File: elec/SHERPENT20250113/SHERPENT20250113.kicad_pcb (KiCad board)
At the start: 4 copper layers, 99 parts, among them J1 2137160001, J2 Conn_01x02_Socket, J3 Conn_01x03_Socket, J4 Conn_01x03_Socket, Q1 NMOS, Q2 PMOS, SW1 SW_Push, U1 AN034_ANTENNA, U2 MCP73831T-2ACI_OT, U3 TPS61288LRQQR, U4 TPS7A2633DRVR, U5 LM66200DRLR, U6 ESP32-C3, U7 W25Q128JVS, Y1 40MHz

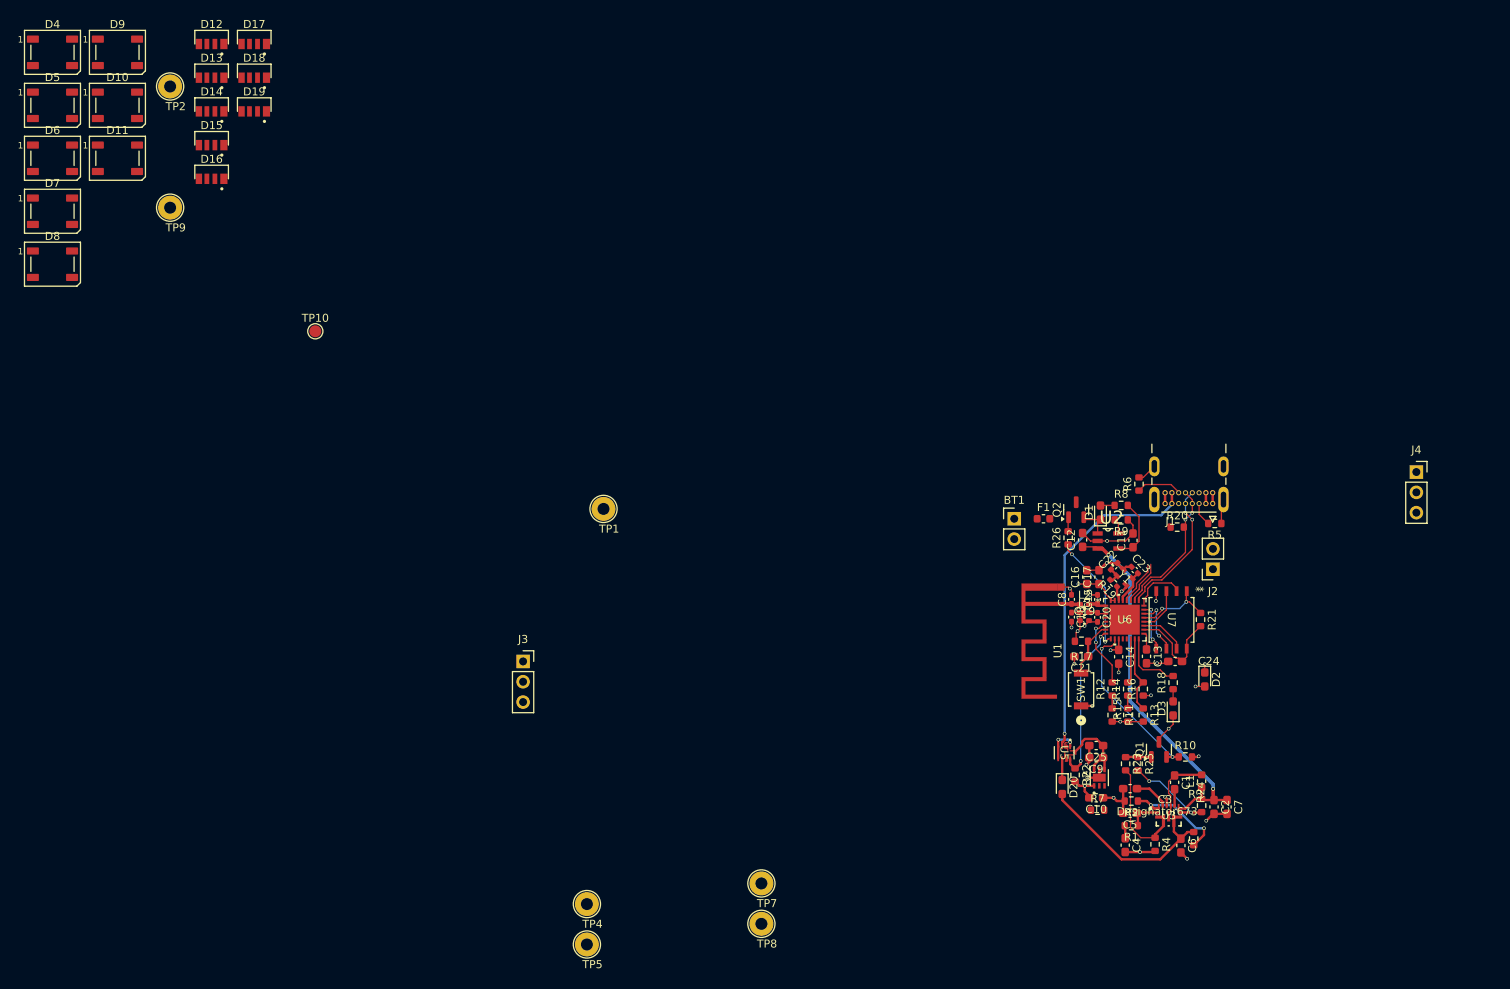
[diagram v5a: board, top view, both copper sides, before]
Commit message: Ajout des LED sur le pcb
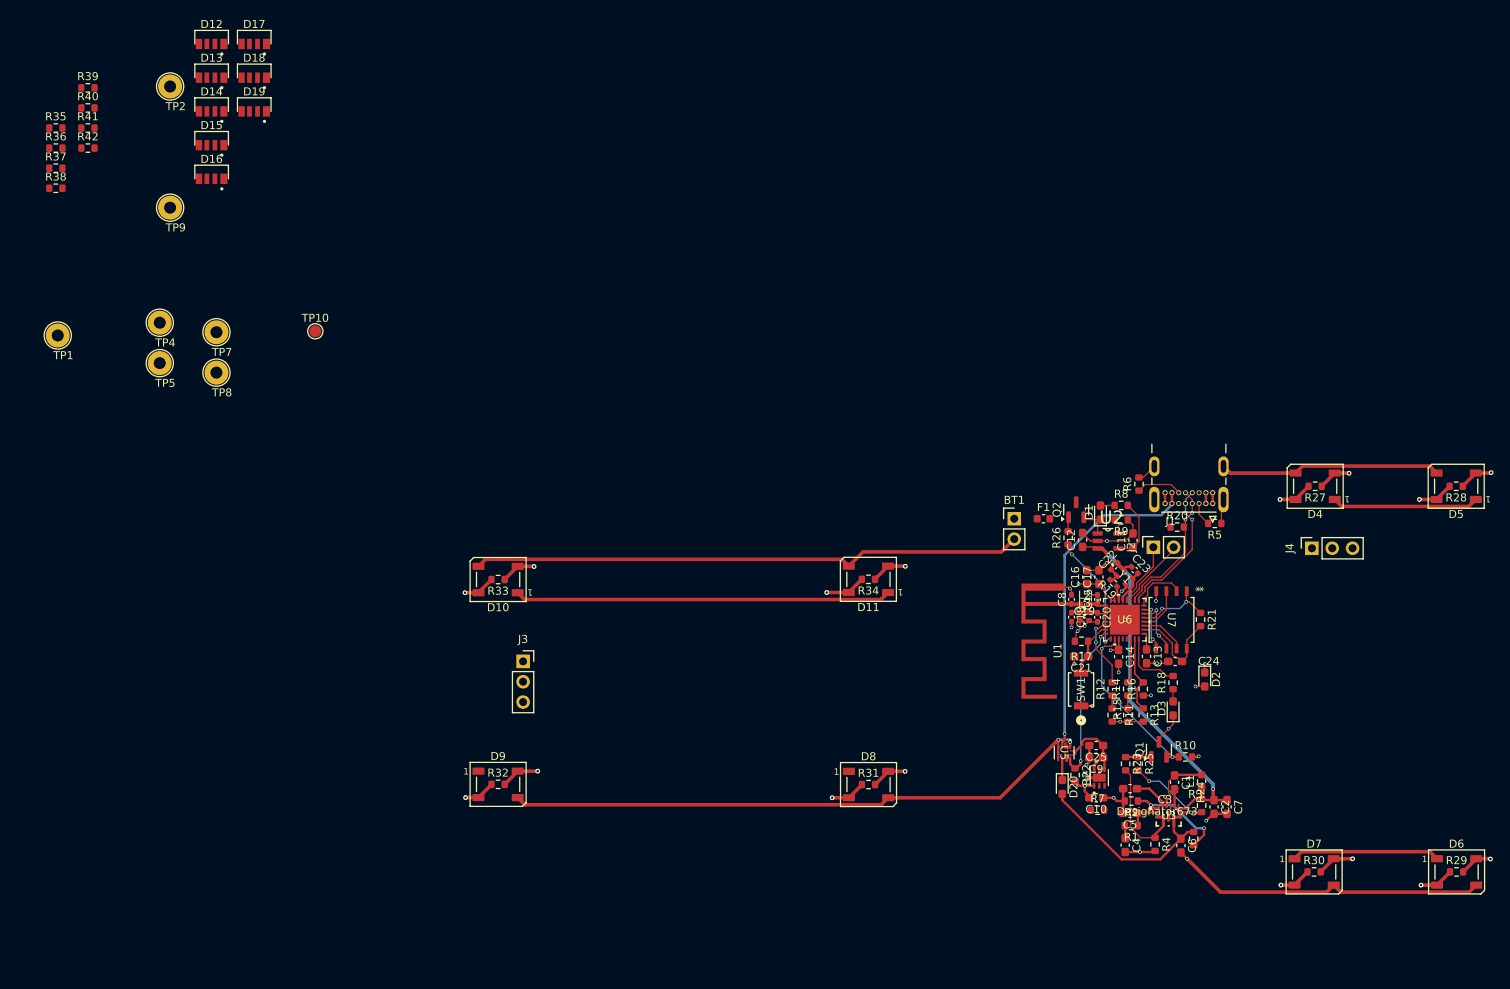
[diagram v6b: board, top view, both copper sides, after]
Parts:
- added R27: 0, Resistor_SMD:R_0603_1608Metric, F.Cu at (184.1, 78.5)
- added R28: 0, Resistor_SMD:R_0603_1608Metric, F.Cu at (201.7, 78.5)
- added R29: 0, Resistor_SMD:R_0603_1608Metric, F.Cu at (201.8, 126.7)
- added R30: 0, Resistor_SMD:R_0603_1608Metric, F.Cu at (184.0, 126.7)
- added R31: 0, Resistor_SMD:R_0603_1608Metric, F.Cu at (128.3, 115.8)
- added R32: 0, Resistor_SMD:R_0603_1608Metric, F.Cu at (82.0, 115.7)
- added R33: 0, Resistor_SMD:R_0603_1608Metric, F.Cu at (82.0, 90.1)
- added R34: 0, Resistor_SMD:R_0603_1608Metric, F.Cu at (128.3, 90.1)
- added R35: 0, Resistor_SMD:R_0603_1608Metric, F.Cu at (26.7, 33.7)
- added R36: 0, Resistor_SMD:R_0603_1608Metric, F.Cu at (26.7, 36.2)
- added R37: 0, Resistor_SMD:R_0603_1608Metric, F.Cu at (26.7, 38.7)
- added R38: 0, Resistor_SMD:R_0603_1608Metric, F.Cu at (26.7, 41.2)
- added R39: 0, Resistor_SMD:R_0603_1608Metric, F.Cu at (30.7, 28.7)
- added R40: 0, Resistor_SMD:R_0603_1608Metric, F.Cu at (30.7, 31.2)
- added R41: 0, Resistor_SMD:R_0603_1608Metric, F.Cu at (30.7, 33.7)
- added R42: 0, Resistor_SMD:R_0603_1608Metric, F.Cu at (30.7, 36.2)
- moved D6 196.9 mm to (201.8, 126.7)
- moved D5 181.8 mm to (201.7, 78.5), turned to 180 degrees
- moved D7 178.0 mm to (184.0, 126.7)
- moved D4 166.9 mm to (184.1, 78.5), turned to 180 degrees
- moved D8 121.0 mm to (128.3, 115.8)
- moved D11 107.6 mm to (128.3, 90.1), turned to 180 degrees
- moved D9 103.1 mm to (82.0, 115.7)
- moved TP7 96.9 mm to (46.8, 59.2)
- moved TP8 96.9 mm to (46.8, 64.3)
- moved TP4 90.2 mm to (39.7, 58.0)
- moved TP5 90.2 mm to (39.7, 63.1)
- moved D10 76.0 mm to (82.0, 90.1), turned to 180 degrees
- moved TP1 71.6 mm to (26.9, 59.6)
- moved J4 16.2 mm to (183.7, 86.2), turned to 90 degrees
- moved J2 7.94 mm to (163.9, 86.1), turned to 90 degrees
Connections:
- D19 pad 3: Net-(D19-DOUT) -> /I2C_DI
- D4 pad 4: /NEO -> /I2C_DO
- TP10 pad 1: Net-(D19-DOUT) -> /I2C_DI
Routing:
- net GND: track 76.5 -> 283.5 mm
- net Net-(D5-DOUT): track 0.00 -> 111.5 mm, vias 0 -> 2
- net +5V: track 0.00 -> 83.9 mm
- net Net-(D7-DOUT): track 0.00 -> 61.4 mm, vias 0 -> 2
- net Net-(D8-DOUT): track 0.00 -> 47.4 mm, vias 0 -> 2
- net Net-(D10-DOUT): track 0.00 -> 47.4 mm, vias 0 -> 2
- net Net-(D10-DIN): track 0.00 -> 33.6 mm, vias 0 -> 2
- net /I2C_DO: track 5.56 -> 28.9 mm, vias 0 -> 1
- net Net-(D6-DOUT): track 0.00 -> 18.9 mm, vias 0 -> 2
- net Net-(D4-DOUT): track 0.00 -> 18.7 mm, vias 0 -> 2
- net Net-(D11-DOUT): track 0.00 -> 4.50 mm, vias 0 -> 1
- net /I2C_DI: track 5.52 -> 8.35 mm

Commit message: Ajout de step
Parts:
- removed D12, D13, D14, D15, D16, D17, D18, D19: WS2812B4020, Library:WS2812B4020
- removed R35, R36, R37, R38, R39, R40, R41, R42: 0, Resistor_SMD:R_0603_1608Metric
- removed TP1, TP2, TP4, TP5, TP7, TP8, TP9: TestPoint, TestPoint:TestPoint_Loop_D2.54mm_Drill1.5mm_Beaded
- removed TP10: TestPoint, TestPoint:TestPoint_Pad_D1.5mm
- added REF**: MountingHole_3.5mm, MountingHole:MountingHole_3.5mm, F.Cu at (139.0, 129.0)
- added REF**: MountingHole_3.5mm, MountingHole:MountingHole_3.5mm, F.Cu at (157.0, 129.0)
- added REF**: MountingHole_3.5mm, MountingHole:MountingHole_3.5mm, F.Cu at (139.0, 77.0)
- added REF**: MountingHole_3.5mm, MountingHole:MountingHole_3.5mm, F.Cu at (157.0, 77.0)
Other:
- board outline added: 130.2 x 60.2 mm

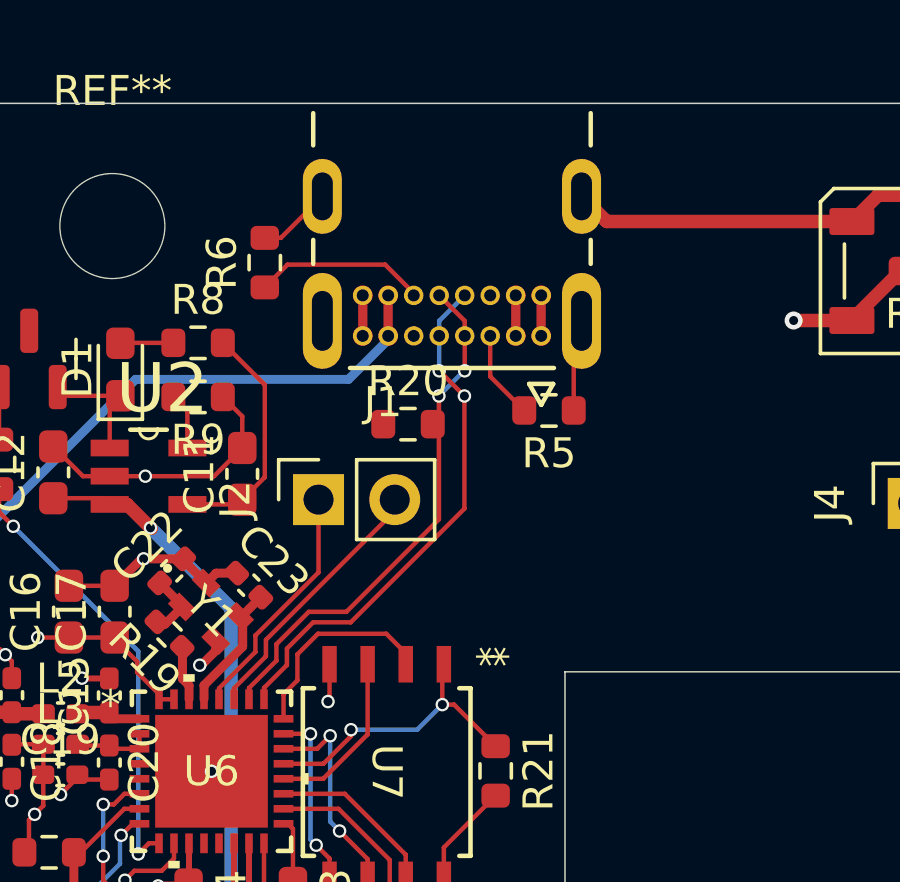
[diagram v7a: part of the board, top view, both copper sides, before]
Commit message: Changer le connecteur usb de côté
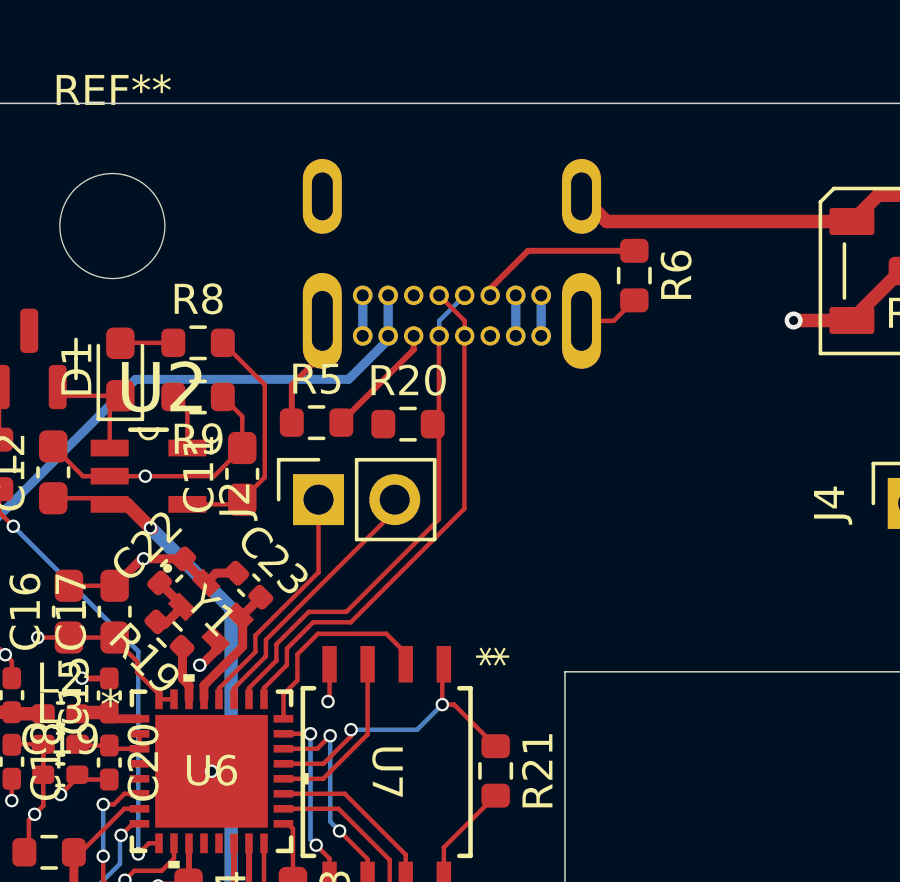
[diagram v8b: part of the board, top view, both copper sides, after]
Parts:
- J1: moved to B.Cu
- moved R6 12.3 mm to (174.4, 78.6), turned to -90 degrees
- moved R5 7.76 mm to (163.8, 83.5), turned to 0 degrees
- turned J1 to 0 degrees
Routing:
- net Net-(J1-CC1): track 2.96 -> 3.89 mm
- net GND: track 283.5 -> 284.2 mm
- net /USB_ESP32P: track 17.5 -> 17.2 mm, vias 2 -> 0
- net /USB_ESP32N: track 17.7 -> 17.3 mm, vias 2 -> 0
